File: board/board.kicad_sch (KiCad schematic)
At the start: 24 parts, among them J1 port attiny, J10 BMS Bat +, J11 BMS Bat gnd, J12 BMS out -, J13 BMS in +5v, J14 BMS in gnd, J15 BMS led charge ok, J16 Mp3 D1 led marche ok, J17 Haut parleur, J18 Batterie + et -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

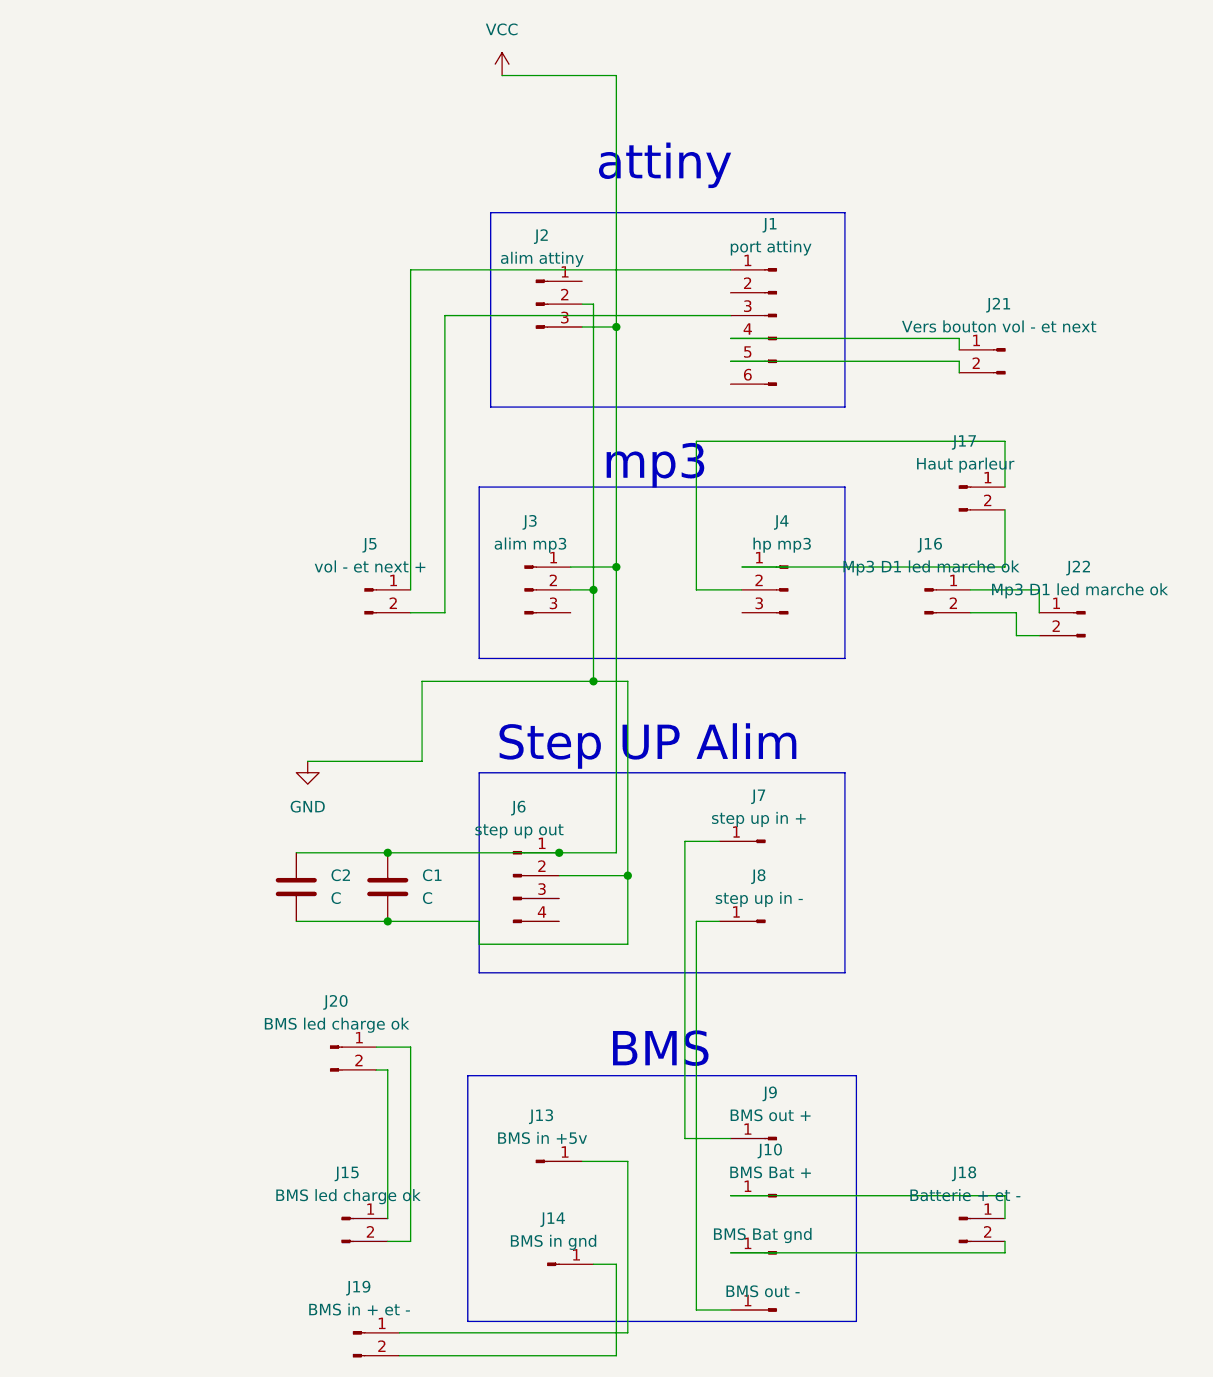
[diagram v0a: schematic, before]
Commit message: ajout +5v + resistance de tirage
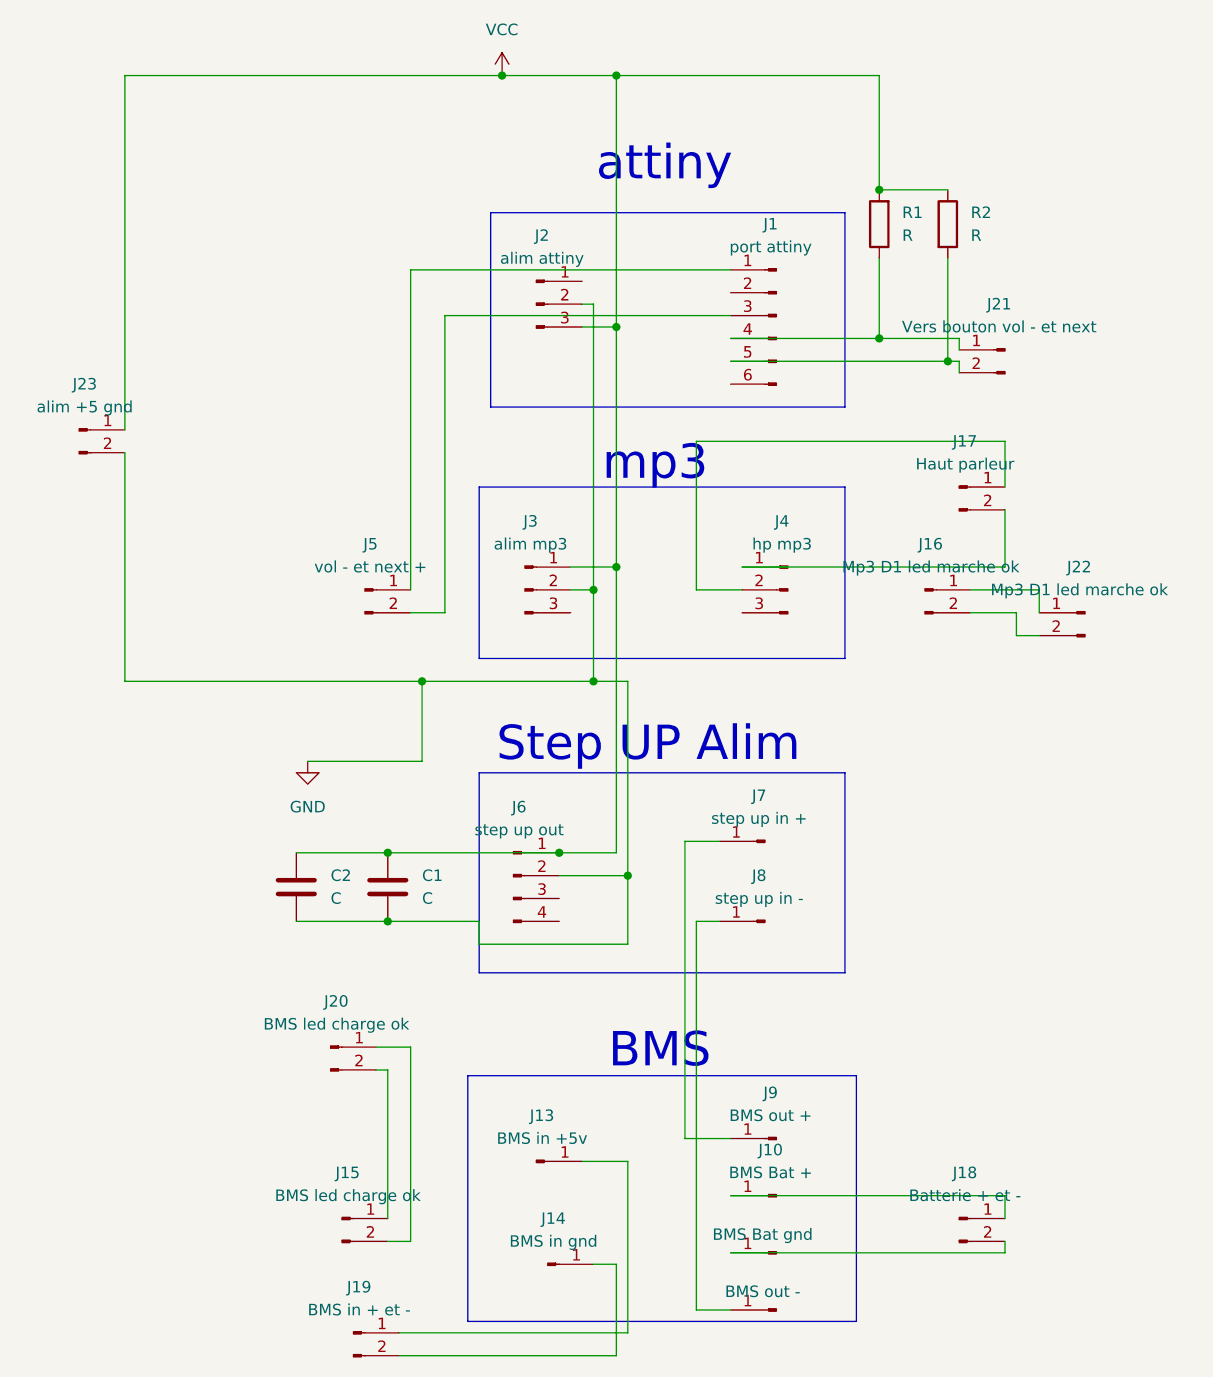
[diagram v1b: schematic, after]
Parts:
- added J23: alim +5 gnd, Connector_PinHeader_2.54mm:PinHeader_1x02_P2.54mm_Vertical, symbol Connector:Conn_01x02_Pin
- added R1, R2: R, Resistor_SMD:R_1206_3216Metric, symbol Device:R
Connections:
- net GND: now also J23.2 (Pin_2)
- net VCC: now also J23.1 (Pin_1), R1.2, R2.1
- net at J1.4 (Pin_4), J21.1 (Pin_1): now also R1.1
- net at J1.5 (Pin_5), J21.2 (Pin_2): now also R2.2

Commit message: pcb carte mere mise a jour
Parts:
- J15_C189893: renamed from J15; footprint Connector_PinSocket_2.54mm:PinSocket_1x02_P2.54mm_Vertical -> Connector_JST:JST_GH_BM02B-GHS-TBT_1x02-1MP_P1.25mm_Vertical
- J16: footprint Connector_PinSocket_2.54mm:PinSocket_1x02_P2.54mm_Vertical -> Connector_PinHeader_2.54mm:PinHeader_1x02_P2.54mm_Vertical
- J17_C189893: renamed from J17; footprint Connector_PinSocket_2.54mm:PinSocket_1x02_P2.54mm_Vertical -> Connector_JST:JST_GH_BM02B-GHS-TBT_1x02-1MP_P1.25mm_Vertical
- J18_C189893: renamed from J18; footprint Connector_PinSocket_2.54mm:PinSocket_1x02_P2.54mm_Vertical -> Connector_JST:JST_GH_BM02B-GHS-TBT_1x02-1MP_P1.25mm_Vertical
- J19_C189893: renamed from J19; footprint Connector_PinSocket_2.54mm:PinSocket_1x02_P2.54mm_Vertical -> Connector_JST:JST_GH_BM02B-GHS-TBT_1x02-1MP_P1.25mm_Vertical
- J21_C189893: renamed from J21; footprint Connector_PinSocket_2.54mm:PinSocket_1x02_P2.54mm_Vertical -> Connector_JST:JST_GH_BM02B-GHS-TBT_1x02-1MP_P1.25mm_Vertical
- J22_C189893: renamed from J22; footprint Connector_PinSocket_2.54mm:PinSocket_1x02_P2.54mm_Vertical -> Connector_JST:JST_GH_BM02B-GHS-TBT_1x02-1MP_P1.25mm_Vertical
- J23-C189893: renamed from J23; footprint Connector_PinHeader_2.54mm:PinHeader_1x02_P2.54mm_Vertical -> Connector_JST:JST_GH_BM02B-GHS-TBT_1x02-1MP_P1.25mm_Vertical
- J5_C189893: renamed from J5; footprint Connector_PinSocket_2.54mm:PinSocket_1x02_P2.54mm_Vertical -> Connector_PinHeader_2.54mm:PinHeader_1x02_P2.54mm_Vertical
- R1, R2: value R -> 4.7kΩ _C2907499
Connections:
- net VCC: now also R1.1; no longer R1.2
- net at J1.4 (Pin_4), J21_C189893.1 (Pin_1): now also R1.2; no longer R1.1
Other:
- moved on the sheet: R1
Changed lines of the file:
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@@
-	)
-	(junction
-		(at 125.73 45.72)
-		(diameter 0)
-		(color 0 0 0 0)
 	)
 	(junction
@@
 	(junction
 		(at 96.52 33.02)
+		(diameter 0)
+		(color 0 0 0 0)
+	)
+	(junction
+		(at 125.73 45.72)
 		(diameter 0)
 		(color 0 0 0 0)
@@
 		(dnp no)
 		(fields_autoplaced yes)
-		(property "Reference" "J23"
+		(property "Reference" "J23-C189893"
 			(at 37.465 67.31 0)
 			(effects
@@
 			)
 		)
-		(property "Footprint" "Connector_PinHeader_2.54mm:PinHeader_1x02_P2.54mm_Vertical"
+		(property "Footprint" "Connector_JST:JST_GH_BM02B-GHS-TBT_1x02-1MP_P1.25mm_Vertical"
 			(at 36.83 72.39 0)
 			(effects
@@
 			(project ""
 				(path "/1d4ba15b-5ce7-48af-a486-6050b996f974"
-					(reference "J23")
+					(reference "J23-C189893")
 					(unit 1)
 				)
@@
 			)
 		)
-		(property "Value" "R"
+		(property "Value" "4.7kΩ _C2907499"
 			(at 135.89 50.7999 0)
 			(effects
@@
 		(dnp no)
 		(fields_autoplaced yes)
-		(property "Reference" "J15"
+		(property "Reference" "J15_C189893"
 			(at 66.675 154.94 0)
 			(effects
@@
 			)
 		)
-		(property "Footprint" "Connector_PinSocket_2.54mm:PinSocket_1x02_P2.54mm_Vertical"
+		(property "Footprint" "Connector_JST:JST_GH_BM02B-GHS-TBT_1x02-1MP_P1.25mm_Vertical"
 			(at 66.04 160.02 0)
 			(effects
@@
 			(project "board"
 				(path "/1d4ba15b-5ce7-48af-a486-6050b996f974"
-					(reference "J15")
+					(reference "J15_C189893")
 					(unit 1)
 				)
@@
 		(dnp no)
 		(fields_autoplaced yes)
-		(property "Reference" "J5"
+		(property "Reference" "J5_C189893"
 			(at 69.215 85.09 0)
 			(effects
@@
 			)
 		)
-		(property "Footprint" "Connector_PinSocket_2.54mm:PinSocket_1x02_P2.54mm_Vertical"
+		(property "Footprint" "Connector_PinHeader_2.54mm:PinHeader_1x02_P2.54mm_Vertical"
 			(at 68.58 90.17 0)
 			(effects
@@
 			(project ""
 				(path "/1d4ba15b-5ce7-48af-a486-6050b996f974"
-					(reference "J5")
+					(reference "J5_C189893")
 					(unit 1)
 				)
@@
 	(symbol
 		(lib_id "Device:R")
-		(at 125.73 49.53 180)
+		(at 125.73 49.53 0)
 		(unit 1)
 		(exclude_from_sim no)
@@
 					(size 1.27 1.27)
 				)
-				(justify right)
-			)
-		)
-		(property "Value" "R"
+				(justify left)
+			)
+		)
+		(property "Value" "4.7kΩ _C2907499"
 			(at 128.27 50.7999 0)
 			(effects
@@
 					(size 1.27 1.27)
 				)
-				(justify right)
+				(justify left)
 			)
 		)
 		(property "Footprint" "Resistor_SMD:R_1206_3216Metric"
-			(at 127.508 49.53 90)
+			(at 123.952 49.53 90)
 			(effects
 				(font
@@
 			)
 		)
-		(property "Footprint" "Connector_PinSocket_2.54mm:PinSocket_1x02_P2.54mm_Vertical"
+		(property "Footprint" "Connector_PinHeader_2.54mm:PinHeader_1x02_P2.54mm_Vertical"
 			(at 130.81 90.17 0)
 			(effects
@@
 		(dnp no)
 		(fields_autoplaced yes)
-		(property "Reference" "J21"
+		(property "Reference" "J21_C189893"
 			(at 139.065 58.42 0)
 			(effects
@@
 			)
 		)
-		(property "Footprint" "Connector_PinSocket_2.54mm:PinSocket_1x02_P2.54mm_Vertical"
+		(property "Footprint" "Connector_JST:JST_GH_BM02B-GHS-TBT_1x02-1MP_P1.25mm_Vertical"
 			(at 139.7 63.5 0)
 			(effects
@@
 			(project "board"
 				(path "/1d4ba15b-5ce7-48af-a486-6050b996f974"
-					(reference "J21")
+					(reference "J21_C189893")
 					(unit 1)
 				)
@@
 		(dnp no)
 		(fields_autoplaced yes)
-		(property "Reference" "J19"
+		(property "Reference" "J19_C189893"
 			(at 67.945 167.64 0)
 			(effects
@@
 			)
 		)
-		(property "Footprint" "Connector_PinSocket_2.54mm:PinSocket_1x02_P2.54mm_Vertical"
+		(property "Footprint" "Connector_JST:JST_GH_BM02B-GHS-TBT_1x02-1MP_P1.25mm_Vertical"
 			(at 67.31 172.72 0)
 			(effects
@@
 			(project "board"
 				(path "/1d4ba15b-5ce7-48af-a486-6050b996f974"
-					(reference "J19")
+					(reference "J19_C189893")
 					(unit 1)
 				)
@@
 		(dnp no)
 		(fields_autoplaced yes)
-		(property "Reference" "J17"
+		(property "Reference" "J17_C189893"
 			(at 135.255 73.66 0)
 			(effects
@@
 			)
 		)
-		(property "Footprint" "Connector_PinSocket_2.54mm:PinSocket_1x02_P2.54mm_Vertical"
+		(property "Footprint" "Connector_JST:JST_GH_BM02B-GHS-TBT_1x02-1MP_P1.25mm_Vertical"
 			(at 134.62 78.74 0)
 			(effects
@@
 			(project "board"
 				(path "/1d4ba15b-5ce7-48af-a486-6050b996f974"
-					(reference "J17")
+					(reference "J17_C189893")
 					(unit 1)
 				)
@@
 		(dnp no)
 		(fields_autoplaced yes)
-		(property "Reference" "J18"
+		(property "Reference" "J18_C189893"
 			(at 135.255 154.94 0)
 			(effects
@@
 			)
 		)
-		(property "Footprint" "Connector_PinSocket_2.54mm:PinSocket_1x02_P2.54mm_Vertical"
+		(property "Footprint" "Connector_JST:JST_GH_BM02B-GHS-TBT_1x02-1MP_P1.25mm_Vertical"
 			(at 134.62 160.02 0)
 			(effects
@@
 			(project "board"
 				(path "/1d4ba15b-5ce7-48af-a486-6050b996f974"
-					(reference "J18")
+					(reference "J18_C189893")
 					(unit 1)
 				)
@@
 		(dnp no)
 		(fields_autoplaced yes)
-		(property "Reference" "J22"
+		(property "Reference" "J22_C189893"
 			(at 147.955 87.63 0)
 			(effects
@@
 			)
 		)
-		(property "Footprint" "Connector_PinSocket_2.54mm:PinSocket_1x02_P2.54mm_Vertical"
+		(property "Footprint" "Connector_JST:JST_GH_BM02B-GHS-TBT_1x02-1MP_P1.25mm_Vertical"
 			(at 148.59 92.71 0)
 			(effects
@@
 			(project "board"
 				(path "/1d4ba15b-5ce7-48af-a486-6050b996f974"
-					(reference "J22")
+					(reference "J22_C189893")
 					(unit 1)
 				)
